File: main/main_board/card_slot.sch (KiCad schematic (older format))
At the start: 5 parts, among them P1 my_pcie_8x

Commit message: Schematic is mostly complete (except for BIST DACs), and passes ERC.  Rough placement of components on PCB.
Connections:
- net GNDA is gone; now on net GND: P1.A29, P1.A30, P1.A31, P1.A32, P1.A33, P1.A34, P1.A35, P1.A41, P1.A44, P1.A47, P1.B29, P1.B30, P1.B31, P1.B32, P1.B33, P1.B34, P1.B35, P1.B41, P1.B42, P1.B43, P1.B44, P1.B47
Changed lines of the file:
@@
 $Descr A4 11693 8268
 encoding utf-8
-Sheet 10 12
+Sheet 7 12
 Title ""
 Date ""
@@
 $EndComp
 $Comp
-L power:GNDA #PWR0129
-U 1 1 5EC152A3
-P 7450 3750
-AR Path="/5E525F2C/5E59D3A2/5EC152A3" Ref="#PWR0129"  Part="1"
-AR Path="/5E525F2C/5E76A42A/5EC152A3" Ref="#PWR?"  Part="1"
-AR Path="/5E525F2C/5E76E218/5EC152A3" Ref="#PWR?"  Part="1"
-AR Path="/5E525F2C/5E7721D1/5EC152A3" Ref="#PWR?"  Part="1"
-AR Path="/5E525FFE/5EBAAEAF/5EC152A3" Ref="#PWR081"  Part="1"
-AR Path="/5E525FFE/5EBAAF7D/5EC152A3" Ref="#PWR087"  Part="1"
-AR Path="/5E525FFE/5EBAAF8F/5EC152A3" Ref="#PWR093"  Part="1"
-AR Path="/5E525FFE/5EBAAFA1/5EC152A3" Ref="#PWR099"  Part="1"
-F 0 "#PWR099" H 7450 3500 50  0001 C CNN
-F 1 "GNDA" H 7600 3700 50  0000 C CNN
-F 2 "" H 7450 3750 50  0001 C CNN
-F 3 "" H 7450 3750 50  0001 C CNN
-	1    7450 3750
-	1    0    0    -1
-$EndComp
-$Comp
 L ilemt_input:my_pcie_8x P1
 U 3 1 5E67C68B
@@
 Wire Wire Line
 	7450 3750 7200 3750
-$Comp
-L power:GNDA #PWR0161
-U 1 1 5E625DEC
-P 6050 3750
-AR Path="/5E525F2C/5E59D3A2/5E625DEC" Ref="#PWR0161"  Part="1"
-AR Path="/5E525F2C/5E76A42A/5E625DEC" Ref="#PWR?"  Part="1"
-AR Path="/5E525F2C/5E76E218/5E625DEC" Ref="#PWR?"  Part="1"
-AR Path="/5E525F2C/5E7721D1/5E625DEC" Ref="#PWR?"  Part="1"
-AR Path="/5E525FFE/5EBAAEAF/5E625DEC" Ref="#PWR078"  Part="1"
-AR Path="/5E525FFE/5EBAAF7D/5E625DEC" Ref="#PWR084"  Part="1"
-AR Path="/5E525FFE/5EBAAF8F/5E625DEC" Ref="#PWR090"  Part="1"
-AR Path="/5E525FFE/5EBAAFA1/5E625DEC" Ref="#PWR096"  Part="1"
-F 0 "#PWR096" H 6050 3500 50  0001 C CNN
-F 1 "GNDA" H 5900 3700 50  0000 C CNN
-F 2 "" H 6050 3750 50  0001 C CNN
-F 3 "" H 6050 3750 50  0001 C CNN
-	1    6050 3750
-	1    0    0    -1
-$EndComp
 Wire Wire Line
 	6050 3750 6300 3750
@@
 Wire Wire Line
 	5800 6150 5800 6250
+$Comp
+L power:GND #PWR?
+U 1 1 5F68DA1B
+P 6050 3750
+AR Path="/5E525F2C/5E59D3A2/5F68DA1B" Ref="#PWR?"  Part="1"
+AR Path="/5E525F2C/5E76A42A/5F68DA1B" Ref="#PWR?"  Part="1"
+AR Path="/5E525F2C/5E76E218/5F68DA1B" Ref="#PWR?"  Part="1"
+AR Path="/5E525F2C/5E7721D1/5F68DA1B" Ref="#PWR?"  Part="1"
+AR Path="/5E525FFE/5EBAAEAF/5F68DA1B" Ref="#PWR0104"  Part="1"
+AR Path="/5E525FFE/5EBAAF7D/5F68DA1B" Ref="#PWR0111"  Part="1"
+AR Path="/5E525FFE/5EBAAF8F/5F68DA1B" Ref="#PWR0114"  Part="1"
+AR Path="/5E525FFE/5EBAAFA1/5F68DA1B" Ref="#PWR0116"  Part="1"
+F 0 "#PWR0116" H 6050 3500 50  0001 C CNN
+F 1 "GND" H 6050 3600 50  0000 C CNN
+F 2 "" H 6050 3750 50  0001 C CNN
+F 3 "" H 6050 3750 50  0001 C CNN
+	1    6050 3750
+	1    0    0    -1
+$EndComp
+$Comp
+L power:GND #PWR?
+U 1 1 5F694E6E
+P 7450 3750
+AR Path="/5E525F2C/5E59D3A2/5F694E6E" Ref="#PWR?"  Part="1"
+AR Path="/5E525F2C/5E76A42A/5F694E6E" Ref="#PWR?"  Part="1"
+AR Path="/5E525F2C/5E76E218/5F694E6E" Ref="#PWR?"  Part="1"
+AR Path="/5E525F2C/5E7721D1/5F694E6E" Ref="#PWR?"  Part="1"
+AR Path="/5E525FFE/5EBAAEAF/5F694E6E" Ref="#PWR0107"  Part="1"
+AR Path="/5E525FFE/5EBAAF7D/5F694E6E" Ref="#PWR0113"  Part="1"
+AR Path="/5E525FFE/5EBAAF8F/5F694E6E" Ref="#PWR0115"  Part="1"
+AR Path="/5E525FFE/5EBAAFA1/5F694E6E" Ref="#PWR0117"  Part="1"
+F 0 "#PWR0117" H 7450 3500 50  0001 C CNN
+F 1 "GND" H 7450 3600 50  0000 C CNN
+F 2 "" H 7450 3750 50  0001 C CNN
+F 3 "" H 7450 3750 50  0001 C CNN
+	1    7450 3750
+	1    0    0    -1
+$EndComp
 $EndSCHEMATC

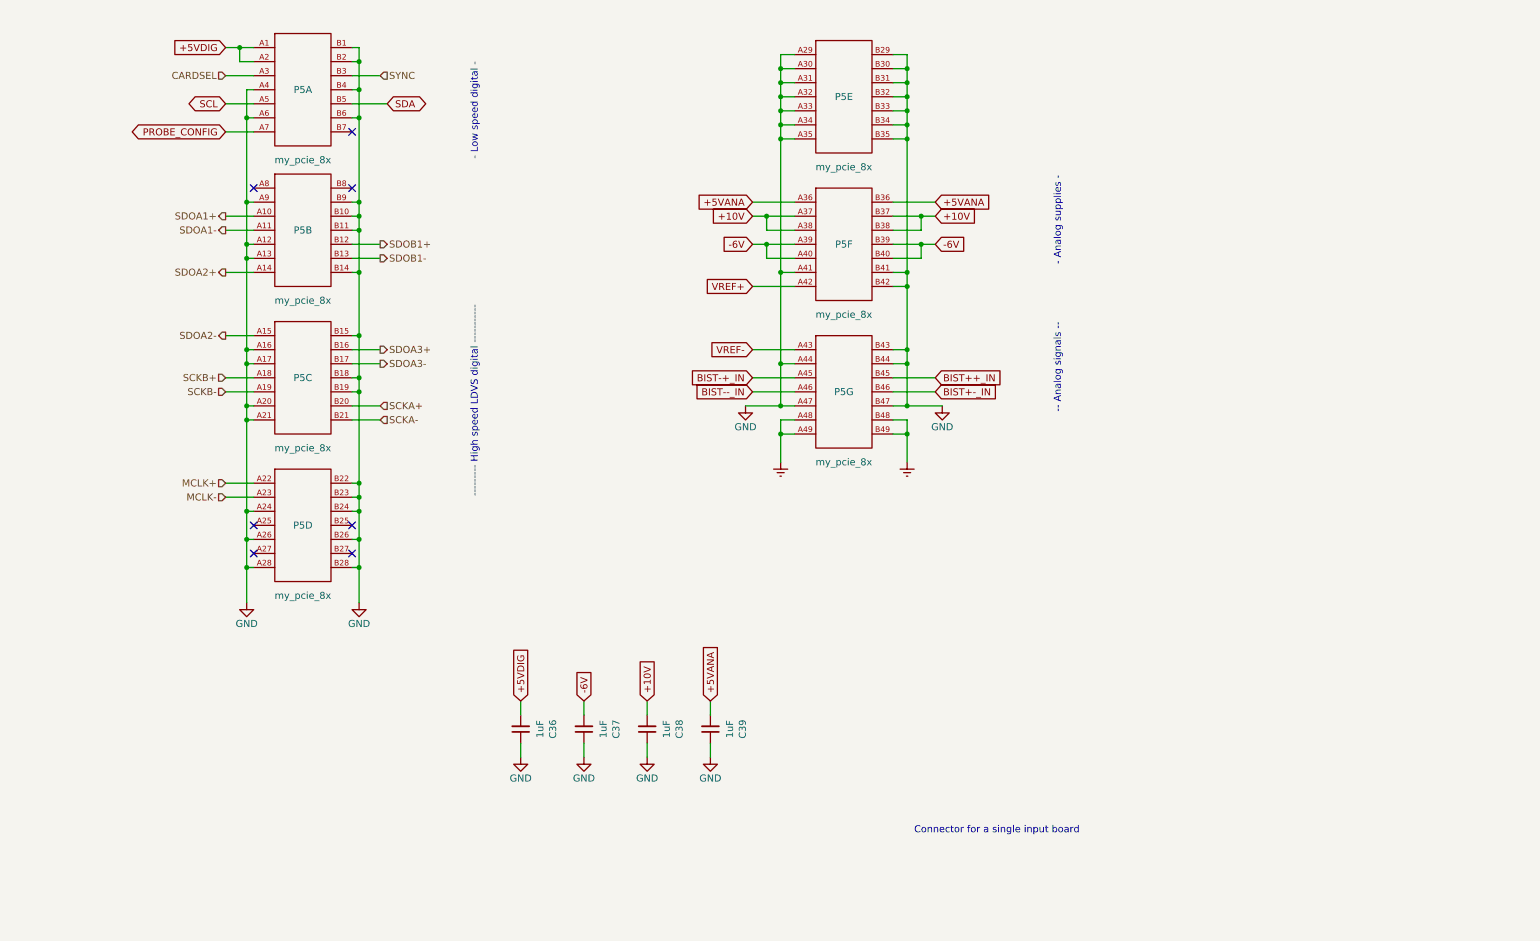
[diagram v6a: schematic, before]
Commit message: Mechanical feature layout on main board (edge connector and mount hole locations).  Added some dimension callouts to the input board. Tweaked grounding on main board schematic.  Chassis ground is not connected to main board ground except via an optional capacitor.  Chassis ground comes in on the power connector. Added BIST DAC, including additions to power.sch and input_slots.sch.
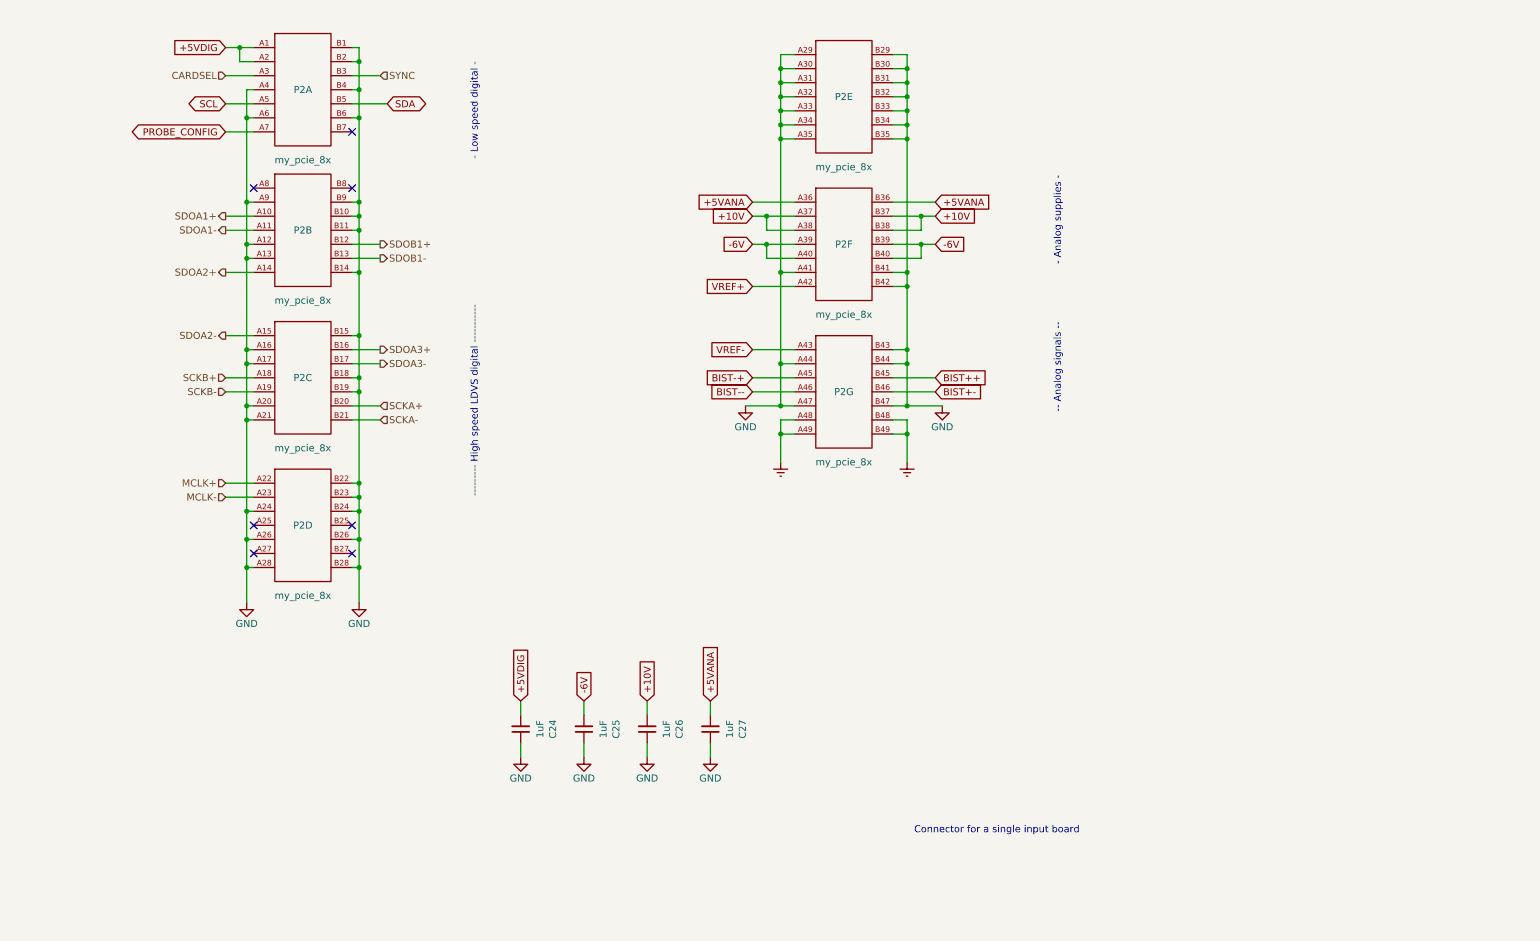
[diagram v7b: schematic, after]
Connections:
- net BIST++_IN renamed BIST++
- net BIST+-_IN renamed BIST+-
- net BIST-+_IN renamed BIST-+
- net BIST--_IN renamed BIST--
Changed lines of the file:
@@
 +5VANA
 Text GLabel 7400 3550 2    50   Input ~ 0
-BIST++_IN
+BIST++
 Text GLabel 7400 3650 2    50   Input ~ 0
-BIST+-_IN
+BIST+-
 Text GLabel 7400 2400 2    50   Input ~ 0
 +10V
@@
 AR Path="/5E525FFE/5EBAAF8F/5E67C68B" Ref="P4"  Part="3"
 AR Path="/5E525FFE/5EBAAFA1/5E67C68B" Ref="P5"  Part="3"
-F 0 "P5" H 2900 3550 50  0000 C CNN
+F 0 "P2" H 2900 3550 50  0000 C CNN
 F 1 "my_pcie_8x" H 2900 3050 50  0000 C CNN
 F 2 "input:PCIE_8x_female" H 2900 4050 50  0001 C CNN
@@
 AR Path="/5E525FFE/5EBAAF8F/5E682A6A" Ref="P4"  Part="5"
 AR Path="/5E525FFE/5EBAAFA1/5E682A6A" Ref="P5"  Part="5"
-F 0 "P5" H 6750 1550 50  0000 C CNN
+F 0 "P2" H 6750 1550 50  0000 C CNN
 F 1 "my_pcie_8x" H 6750 1050 50  0000 C CNN
 F 2 "input:PCIE_8x_female" H 6750 2050 50  0001 C CNN
@@
 AR Path="/5E525FFE/5EBAAF8F/5E625DE8" Ref="P4"  Part="6"
 AR Path="/5E525FFE/5EBAAFA1/5E625DE8" Ref="P5"  Part="6"
-F 0 "P5" H 6750 2600 50  0000 C CNN
+F 0 "P2" H 6750 2600 50  0000 C CNN
 F 1 "my_pcie_8x" H 6750 2100 50  0000 C CNN
 F 2 "input:PCIE_8x_female" H 6750 3100 50  0001 C CNN
@@
 AR Path="/5E525FFE/5EBAAF8F/5E625DE9" Ref="P4"  Part="7"
 AR Path="/5E525FFE/5EBAAFA1/5E625DE9" Ref="P5"  Part="7"
-F 0 "P5" H 6750 3650 50  0000 C CNN
+F 0 "P2" H 6750 3650 50  0000 C CNN
 F 1 "my_pcie_8x" H 6750 3150 50  0000 C CNN
 F 2 "input:PCIE_8x_female" H 6750 4150 50  0001 C CNN
@@
 AR Path="/5E525FFE/5EBAAF8F/5EC152A6" Ref="P4"  Part="2"
 AR Path="/5E525FFE/5EBAAFA1/5EC152A6" Ref="P5"  Part="2"
-F 0 "P5" H 2900 2500 50  0000 C CNN
+F 0 "P2" H 2900 2500 50  0000 C CNN
 F 1 "my_pcie_8x" H 2900 2000 50  0000 C CNN
 F 2 "input:PCIE_8x_female" H 2900 3000 50  0001 C CNN
@@
 	7400 3650 7100 3650
 Text GLabel 6100 3650 0    50   Input ~ 0
-BIST--_IN
+BIST--
 Text GLabel 6100 3550 0    50   Input ~ 0
-BIST-+_IN
+BIST-+
 Wire Wire Line
 	6100 3550 6400 3550
@@
 AR Path="/5E525FFE/5EBAAF8F/5E681104" Ref="P4"  Part="1"
 AR Path="/5E525FFE/5EBAAFA1/5E681104" Ref="P5"  Part="1"
-F 0 "P5" H 2900 1500 50  0000 C CNN
+F 0 "P2" H 2900 1500 50  0000 C CNN
 F 1 "my_pcie_8x" H 2900 1000 50  0000 C CNN
 F 2 "input:PCIE_8x_female" H 2900 2000 50  0001 C CNN
@@
 AR Path="/5E525FFE/5EBAAF8F/5EC152A7" Ref="P4"  Part="4"
 AR Path="/5E525FFE/5EBAAFA1/5EC152A7" Ref="P5"  Part="4"
-F 0 "P5" H 2900 4600 50  0000 C CNN
+F 0 "P2" H 2900 4600 50  0000 C CNN
 F 1 "my_pcie_8x" H 2900 4100 50  0000 C CNN
 F 2 "input:PCIE_8x_female" H 2900 5100 50  0001 C CNN
@@
 AR Path="/5E525FFE/5EBAAF8F/5ED81315" Ref="C32"  Part="1"
 AR Path="/5E525FFE/5EBAAFA1/5ED81315" Ref="C36"  Part="1"
-F 0 "C36" V 4221 6050 50  0000 C CNN
+F 0 "C24" V 4221 6050 50  0000 C CNN
 F 1 "1uF" V 4312 6050 50  0000 C CNN
 F 2 "Capacitor_SMD:C_0805_2012Metric" H 4450 6050 50  0001 C CNN
@@
 AR Path="/5E525FFE/5EBAAF8F/5EDA5F14" Ref="C33"  Part="1"
 AR Path="/5E525FFE/5EBAAFA1/5EDA5F14" Ref="C37"  Part="1"
-F 0 "C37" V 4671 6050 50  0000 C CNN
+F 0 "C25" V 4671 6050 50  0000 C CNN
 F 1 "1uF" V 4762 6050 50  0000 C CNN
 F 2 "Capacitor_SMD:C_0805_2012Metric" H 4900 6050 50  0001 C CNN
@@
 AR Path="/5E525FFE/5EBAAF8F/5EDBD896" Ref="C34"  Part="1"
 AR Path="/5E525FFE/5EBAAFA1/5EDBD896" Ref="C38"  Part="1"
-F 0 "C38" V 5121 6050 50  0000 C CNN
+F 0 "C26" V 5121 6050 50  0000 C CNN
 F 1 "1uF" V 5212 6050 50  0000 C CNN
 F 2 "Capacitor_SMD:C_0805_2012Metric" H 5350 6050 50  0001 C CNN
@@
 AR Path="/5E525FFE/5EBAAF8F/5EDCC5E2" Ref="C35"  Part="1"
 AR Path="/5E525FFE/5EBAAFA1/5EDCC5E2" Ref="C39"  Part="1"
-F 0 "C39" V 5571 6050 50  0000 C CNN
+F 0 "C27" V 5571 6050 50  0000 C CNN
 F 1 "1uF" V 5662 6050 50  0000 C CNN
 F 2 "Capacitor_SMD:C_0805_2012Metric" H 5800 6050 50  0001 C CNN
